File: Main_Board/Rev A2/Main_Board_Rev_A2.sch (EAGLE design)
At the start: 209 parts, among them J1 90814-0208, J12 22-27-2061-06, J15 1241050-5, J2 90814-0206, J3 90814-0208, J4 5504F1-09S-02A-03, J5 22-05-7048-04, J6 22-05-7048-04, J7 22-05-7058-05, J8 22-05-7048-04, J9 22-05-7028-02, K1 G6K-2G-Y, K2 G6K-2G-Y, K3 G6K-2G-Y, K4 G6K-2G-Y, P1 RB1-125BAG1A, SW1 B3FS-1050, SW2 B3FS-1050, T2 MMBT2907ALT3, U1 LT3686HDDPBF, U10 SN74LVC2G17DBVR, U11 MCP2561-E/SN, U12 TLV313, U2 TPL0401A, U3 SN74LVC3G17DCTR, U4 SN74LVC3G17DCTR, U5 LT3686HDDPBF, U6 LPC1768FBD100, U7 AT24C512C-SSHM-B, U8 SN74LVC3G17DCTR, U9 SN74LVC2G17DBVR, X1 ASE_50, X12 22-05-7028-02, X13 22-05-7028-02, X14 22-05-7038-03, X15 22-05-7038-03, X2 FC-135, X3 ASE-12, X4 MSTBA2, X5 22-05-7028-02, X6 USB3075-30-A, X7 3000, X8 22-05-7028-02

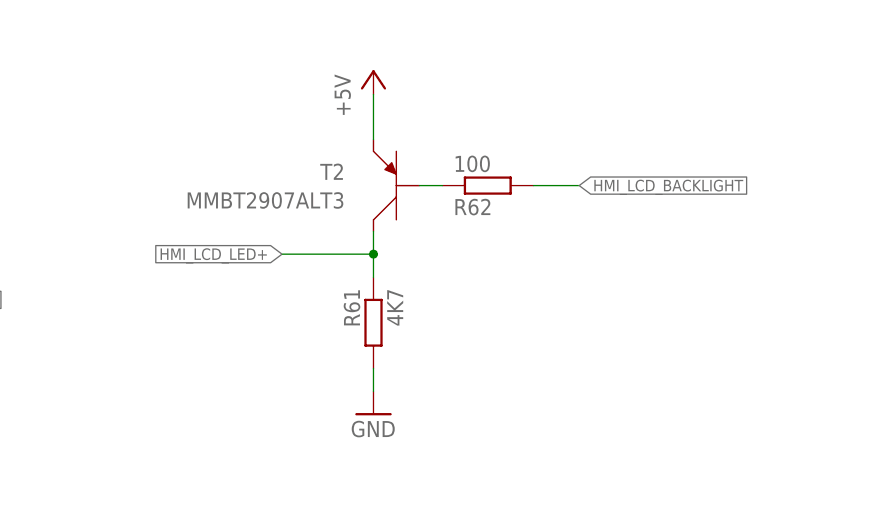
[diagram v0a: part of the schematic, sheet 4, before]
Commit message: Change load pin gain and change to pull-up HMI_LCD_LED+
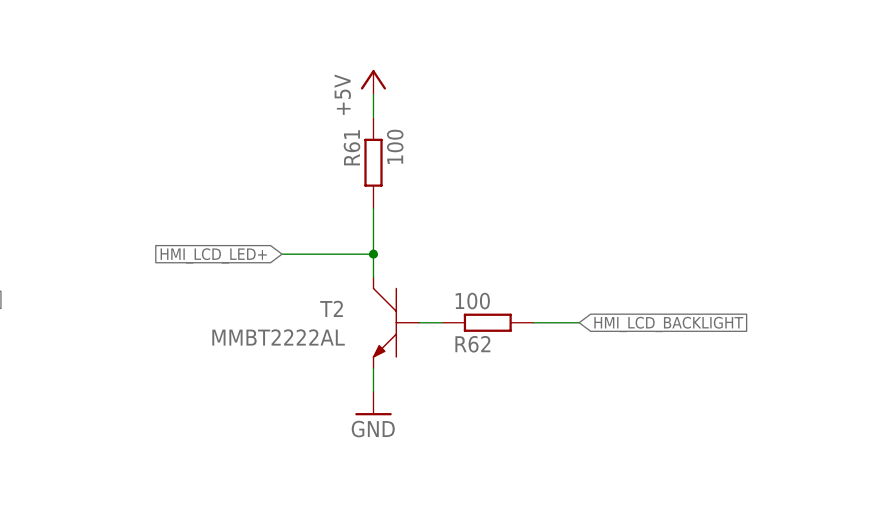
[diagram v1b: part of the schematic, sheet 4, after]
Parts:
- R61: value 4K7 -> 100
- R77, R78: value 150 -> 60.4
- R79, R80: value 100K -> 374K
- T2: value MMBT2907ALT3 -> MMBT2222AL; device transistor:MMBT2907ALT3 -> transistor:MMBT2222AL
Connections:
- net +5V: now also R61.1; no longer T2.C
- net GND: now also T2.E; no longer R61.2
- net HMI_LCD_LED+: now also R61.2, T2.C; no longer R61.1, T2.E
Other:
- moved on the sheet: R61, R62
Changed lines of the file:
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@@
 <attribute name="OC_NEWARK" value="95Y0395"/>
 </part>
-<part name="R77" library="rcl" deviceset="R-EU_" device="R0603" value="150">
+<part name="R77" library="rcl" deviceset="R-EU_" device="R0603" value="60.4">
 <attribute name="MF" value=""/>
 <attribute name="MPN" value="MCMR06X1801FTL"/>
 <attribute name="OC_NEWARK" value="86T3556"/>
 </part>
-<part name="R78" library="rcl" deviceset="R-EU_" device="R0603" value="150">
+<part name="R78" library="rcl" deviceset="R-EU_" device="R0603" value="60.4">
 <attribute name="MF" value=""/>
 <attribute name="MPN" value="MCMR06X1801FTL"/>
 <attribute name="OC_NEWARK" value="86T3556"/>
 </part>
-<part name="R79" library="rcl" deviceset="R-EU_" device="R0603" value="100K">
+<part name="R79" library="rcl" deviceset="R-EU_" device="R0603" value="374K">
 <attribute name="MF" value=""/>
 <attribute name="MPN" value="MCMR06X1201FTL"/>
 <attribute name="OC_NEWARK" value="86T3525"/>
 </part>
-<part name="R80" library="rcl" deviceset="R-EU_" device="R0603" value="100K">
+<part name="R80" library="rcl" deviceset="R-EU_" device="R0603" value="374K">
 <attribute name="MF" value=""/>
 <attribute name="MPN" value="MCMR06X1201FTL"/>
@@
 <part name="GND87" library="supply1" deviceset="GND" device=""/>
 <part name="+3V15" library="supply1" deviceset="+5V" device=""/>
-<part name="T2" library="transistor" deviceset="MMBT2907ALT3" device=""/>
-<part name="R61" library="rcl" deviceset="R-EU_" device="R0603" value="4K7">
+<part name="T2" library="transistor" deviceset="MMBT2222AL" device=""/>
+<part name="R61" library="rcl" deviceset="R-EU_" device="R0603" value="100">
 <attribute name="MF" value=""/>
 <attribute name="MPN" value="MCMR06X33R0FTL"/>
@@
 <attribute name="MPN" x="40.64" y="73.66" size="1.778" layer="96" display="off"/>
 </instance>
-<instance part="T2" gate="G$1" x="332.74" y="231.14" rot="MR0"/>
-<instance part="R61" gate="G$1" x="330.2" y="215.9" rot="MR270">
-<attribute name="OC_NEWARK" x="330.2" y="215.9" size="1.778" layer="96" display="off"/>
-<attribute name="MF" x="330.2" y="215.9" size="1.778" layer="96" display="off"/>
-<attribute name="MPN" x="330.2" y="215.9" size="1.778" layer="96" display="off"/>
+<instance part="T2" gate="1" x="332.74" y="215.9" rot="MR0"/>
+<instance part="R61" gate="G$1" x="330.2" y="233.68" rot="MR270">
+<attribute name="OC_NEWARK" x="330.2" y="233.68" size="1.778" layer="96" display="off"/>
+<attribute name="MF" x="330.2" y="233.68" size="1.778" layer="96" display="off"/>
+<attribute name="MPN" x="330.2" y="233.68" size="1.778" layer="96" display="off"/>
 </instance>
 <instance part="P+23" gate="1" x="330.2" y="243.84"/>
 <instance part="GND98" gate="1" x="330.2" y="205.74"/>
-<instance part="R62" gate="G$1" x="342.9" y="231.14" rot="MR180">
-<attribute name="OC_NEWARK" x="342.9" y="231.14" size="1.778" layer="96" display="off"/>
-<attribute name="MF" x="342.9" y="231.14" size="1.778" layer="96" display="off"/>
-<attribute name="MPN" x="342.9" y="231.14" size="1.778" layer="96" display="off"/>
+<instance part="R62" gate="G$1" x="342.9" y="215.9" rot="MR180">
+<attribute name="OC_NEWARK" x="342.9" y="215.9" size="1.778" layer="96" display="off"/>
+<attribute name="MF" x="342.9" y="215.9" size="1.778" layer="96" display="off"/>
+<attribute name="MPN" x="342.9" y="215.9" size="1.778" layer="96" display="off"/>
 </instance>
 </instances>
@@
 </segment>
 <segment>
-<pinref part="R61" gate="G$1" pin="2"/>
 <pinref part="GND98" gate="1" pin="GND"/>
+<pinref part="T2" gate="1" pin="E"/>
 <wire x1="330.2" y1="208.28" x2="330.2" y2="210.82" width="0.1524" layer="91"/>
 </segment>
@@
 <segment>
 <wire x1="330.2" y1="223.52" x2="320.04" y2="223.52" width="0.1524" layer="91"/>
-<pinref part="T2" gate="G$1" pin="E"/>
-<wire x1="330.2" y1="226.06" x2="330.2" y2="223.52" width="0.1524" layer="91"/>
-<pinref part="R61" gate="G$1" pin="1"/>
-<wire x1="330.2" y1="220.98" x2="330.2" y2="223.52" width="0.1524" layer="91"/>
-<junction x="330.2" y="223.52"/>
 <label x="320.04" y="223.52" size="1.27" layer="95" rot="R180" xref="yes"/>
+<pinref part="R61" gate="G$1" pin="2"/>
+<wire x1="330.2" y1="228.6" x2="330.2" y2="223.52" width="0.1524" layer="91"/>
+<pinref part="T2" gate="1" pin="C"/>
+<wire x1="330.2" y1="223.52" x2="330.2" y2="220.98" width="0.1524" layer="91"/>
+<junction x="330.2" y="223.52"/>
 </segment>
 </net>
@@
 <segment>
 <pinref part="P+23" gate="1" pin="+5V"/>
-<pinref part="T2" gate="G$1" pin="C"/>
-<wire x1="330.2" y1="241.3" x2="330.2" y2="236.22" width="0.1524" layer="91"/>
+<pinref part="R61" gate="G$1" pin="1"/>
+<wire x1="330.2" y1="241.3" x2="330.2" y2="238.76" width="0.1524" layer="91"/>
 </segment>
 </net>
@@
 <net name="HMI_LCD_BACKLIGHT" class="0">
 <segment>
-<wire x1="347.98" y1="231.14" x2="353.06" y2="231.14" width="0.1524" layer="91"/>
-<label x="353.06" y="231.14" size="1.27" layer="95" xref="yes"/>
+<wire x1="347.98" y1="215.9" x2="353.06" y2="215.9" width="0.1524" layer="91"/>
+<label x="353.06" y="215.9" size="1.27" layer="95" xref="yes"/>
 <pinref part="R62" gate="G$1" pin="2"/>
 </segment>
@@
 <net name="N$67" class="0">
 <segment>
-<pinref part="T2" gate="G$1" pin="B"/>
+<pinref part="T2" gate="1" pin="B"/>
 <pinref part="R62" gate="G$1" pin="1"/>
-<wire x1="335.28" y1="231.14" x2="337.82" y2="231.14" width="0.1524" layer="91"/>
+<wire x1="335.28" y1="215.9" x2="337.82" y2="215.9" width="0.1524" layer="91"/>
 </segment>
 </net>

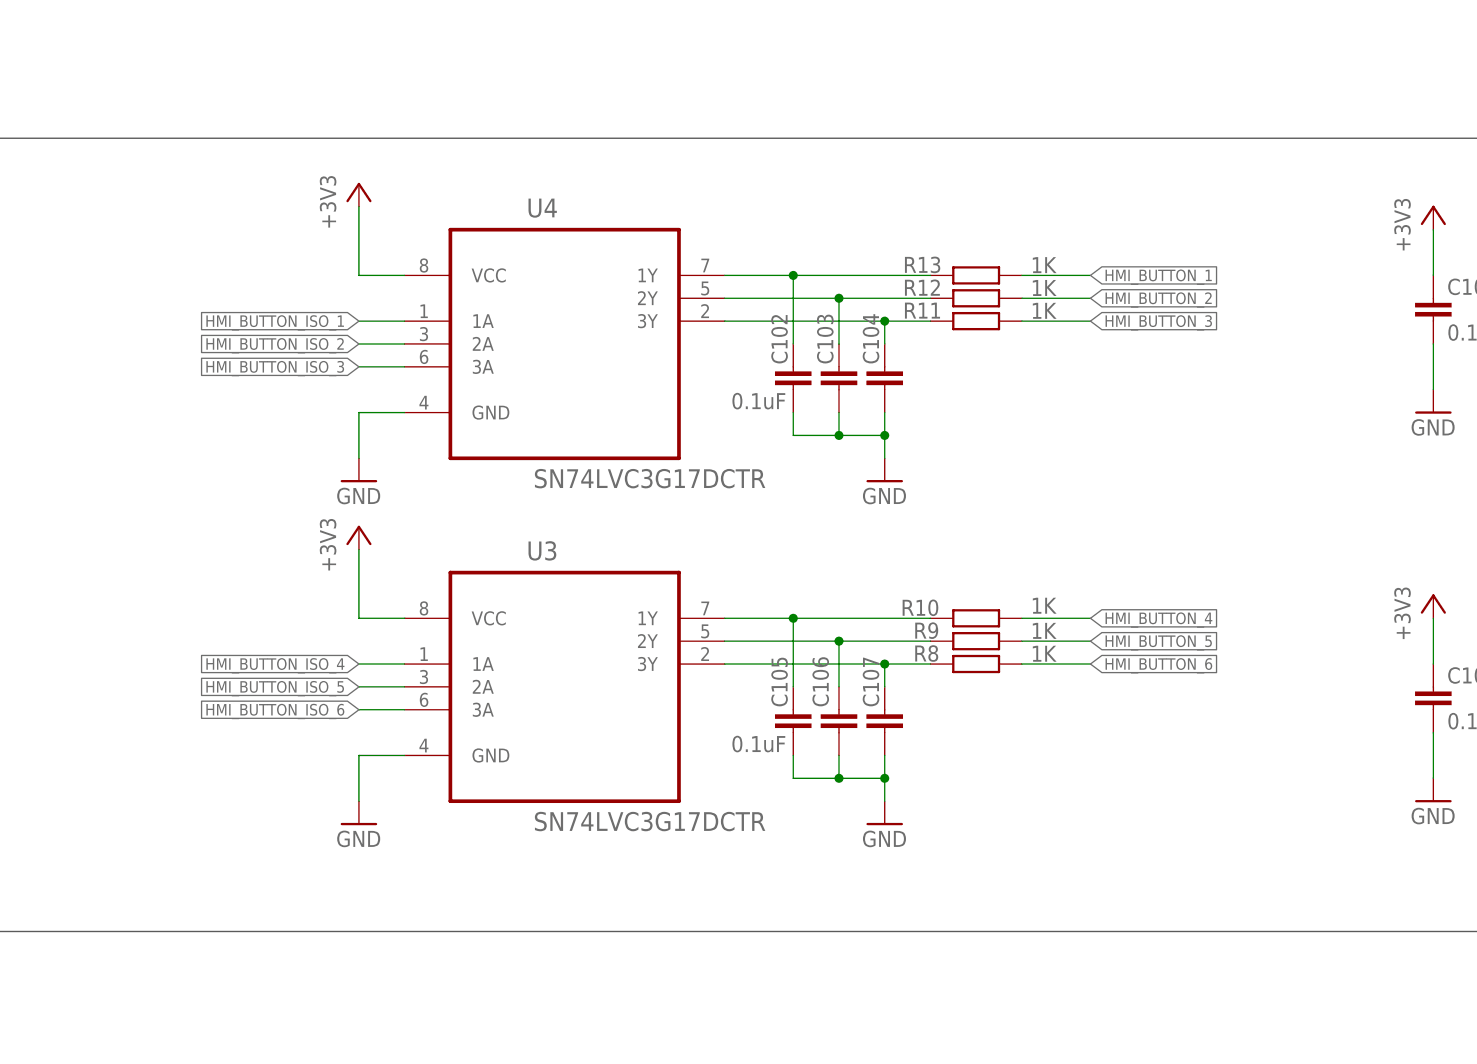
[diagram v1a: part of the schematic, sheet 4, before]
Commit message: nvert IO on U3 and U4 and transistor T1 on pull up output
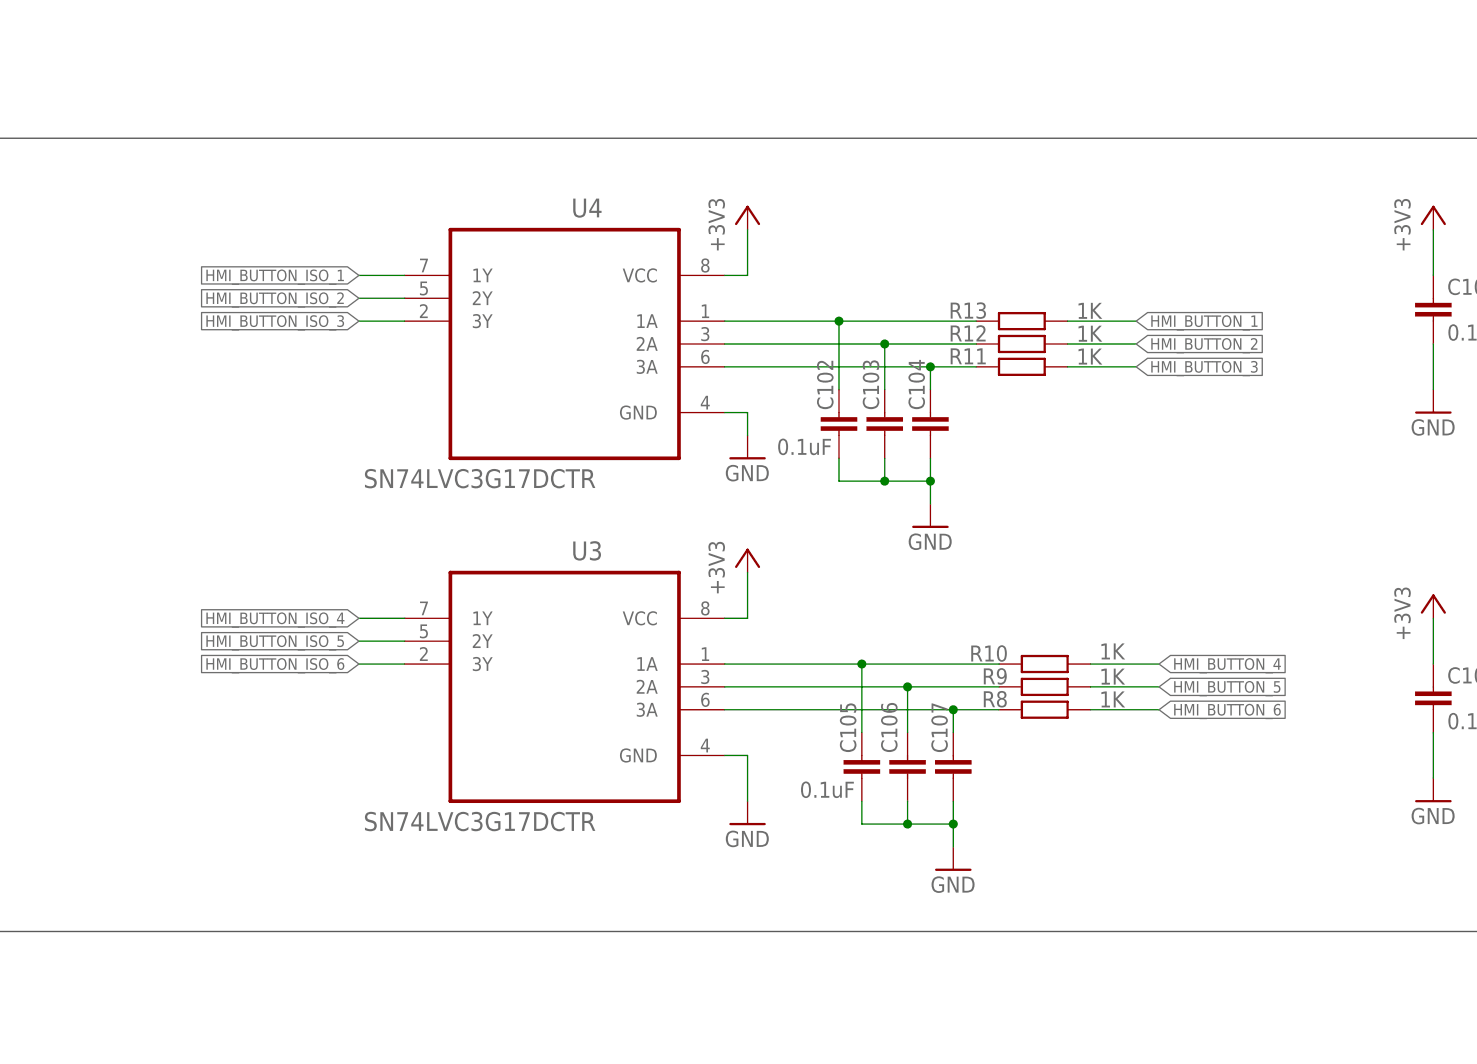
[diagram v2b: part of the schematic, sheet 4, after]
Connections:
- net HMI_BUTTON_ISO_1: now also U4.1Y; no longer U4.1A
- net HMI_BUTTON_ISO_2: now also U4.2Y; no longer U4.2A
- net HMI_BUTTON_ISO_3: now also U4.3Y; no longer U4.3A
- net HMI_BUTTON_ISO_4: now also U3.1Y; no longer U3.1A
- net HMI_BUTTON_ISO_5: now also U3.2Y; no longer U3.2A
- net HMI_BUTTON_ISO_6: now also U3.3Y; no longer U3.3A
- net N$17: now also U4.1A; no longer U4.1Y
- net N$19: now also U4.2A; no longer U4.2Y
- net N$20: now also U4.3A; no longer U4.3Y
- net N$25: now also U3.1A; no longer U3.1Y
- net N$26: now also U3.2A; no longer U3.2Y
- net N$27: now also U3.3A; no longer U3.3Y
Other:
- moved on the sheet: C102, C103, C104, C105, C106, C107, R10, R11, R12, R13, R8, R9

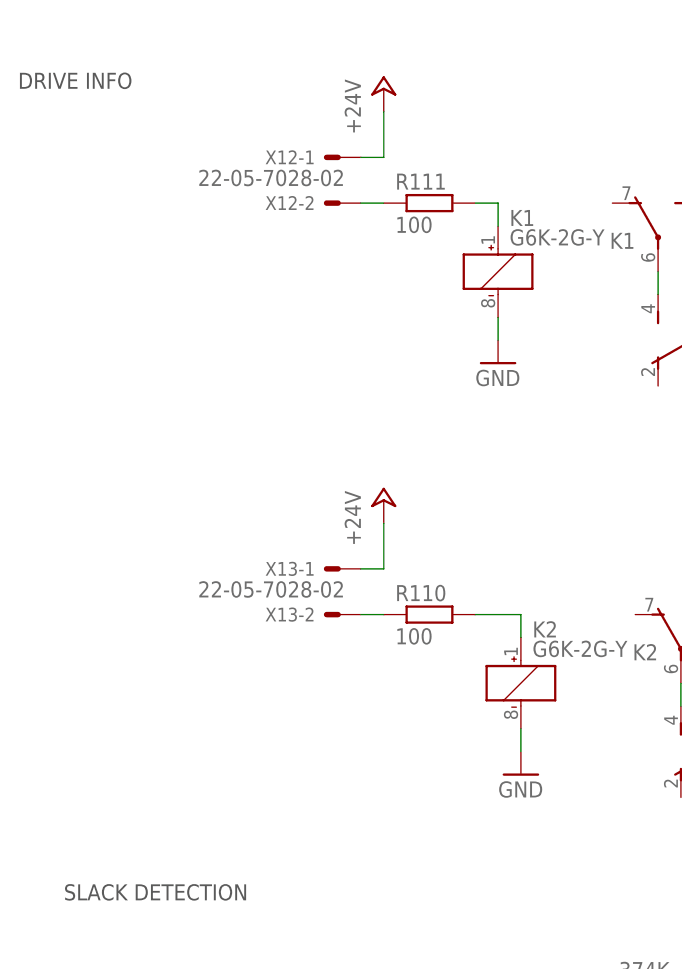
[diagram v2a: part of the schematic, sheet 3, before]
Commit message: Replace Drive error and enable connectors to 3pts molex
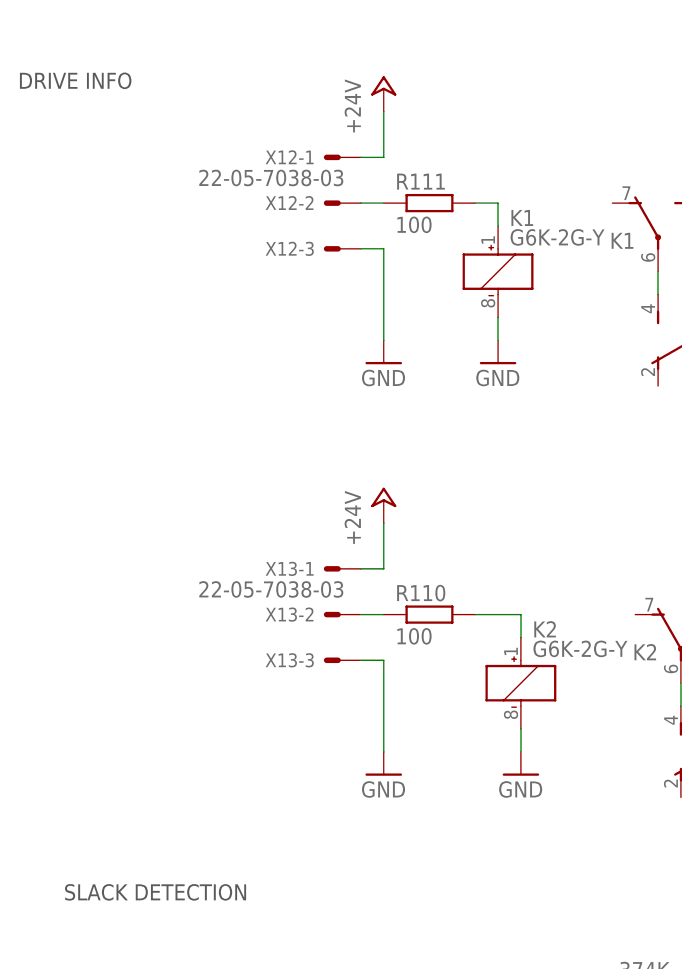
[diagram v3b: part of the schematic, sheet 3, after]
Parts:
- X12, X13: value 22-05-7028-02 -> 22-05-7038-03; device con-molex:22-05-7028-02 -> con-molex:22-05-7038-03
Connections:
- net GND: now also X12-3.S, X13-3.S
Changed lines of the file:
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@@
 <attribute name="OC_NEWARK" value="86T3504"/>
 </part>
-<part name="X12" library="con-molex" deviceset="22-?-02" device="05-7028">
+<part name="X12" library="con-molex" deviceset="22-?-03" device="05-7038">
 <attribute name="MPN" value="22-05-7028"/>
 <attribute name="OC_NEWARK" value="25M1728"/>
@@
 <attribute name="OC_NEWARK" value="86T3504"/>
 </part>
-<part name="X13" library="con-molex" deviceset="22-?-02" device="05-7028">
+<part name="X13" library="con-molex" deviceset="22-?-03" device="05-7038">
 <attribute name="MPN" value="22-05-7028"/>
 <attribute name="OC_NEWARK" value="25M1728"/>
@@
 </part>
 <part name="+3V29" library="supply1" deviceset="+3V3" device=""/>
+<part name="GND88" library="supply1" deviceset="GND" device=""/>
+<part name="GND99" library="supply1" deviceset="GND" device=""/>
 </parts>
 <sheets>
@@
 <instance part="GND97" gate="1" x="100.33" y="7.62"/>
 <instance part="+3V28" gate="G$1" x="73.66" y="49.53"/>
+<instance part="X13" gate="-3" x="40.64" y="91.44" rot="R180"/>
+<instance part="GND88" gate="1" x="45.72" y="78.74"/>
+<instance part="X12" gate="-3" x="40.64" y="137.16" rot="R180"/>
+<instance part="GND99" gate="1" x="45.72" y="124.46"/>
 </instances>
 <busses>
@@
 <wire x1="271.78" y1="121.92" x2="276.86" y2="121.92" width="0.1524" layer="91"/>
 </segment>
+<segment>
+<pinref part="X13" gate="-3" pin="S"/>
+<pinref part="GND88" gate="1" pin="GND"/>
+<wire x1="43.18" y1="91.44" x2="45.72" y2="91.44" width="0.1524" layer="91"/>
+<wire x1="45.72" y1="91.44" x2="45.72" y2="81.28" width="0.1524" layer="91"/>
+</segment>
+<segment>
+<pinref part="X12" gate="-3" pin="S"/>
+<pinref part="GND99" gate="1" pin="GND"/>
+<wire x1="43.18" y1="137.16" x2="45.72" y2="137.16" width="0.1524" layer="91"/>
+<wire x1="45.72" y1="137.16" x2="45.72" y2="127" width="0.1524" layer="91"/>
+</segment>
 </net>
